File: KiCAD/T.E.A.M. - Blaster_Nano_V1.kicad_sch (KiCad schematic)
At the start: 15 parts, among them J1 USB_C_Receptacle_USB2.0_14P, J2 Conn_01x02, J3 Conn_01x02, J4 Conn_01x02, J5 Conn_01x02, Q1 FS8205A, U1 TP4056-42-ESOP8, U2 DW01A

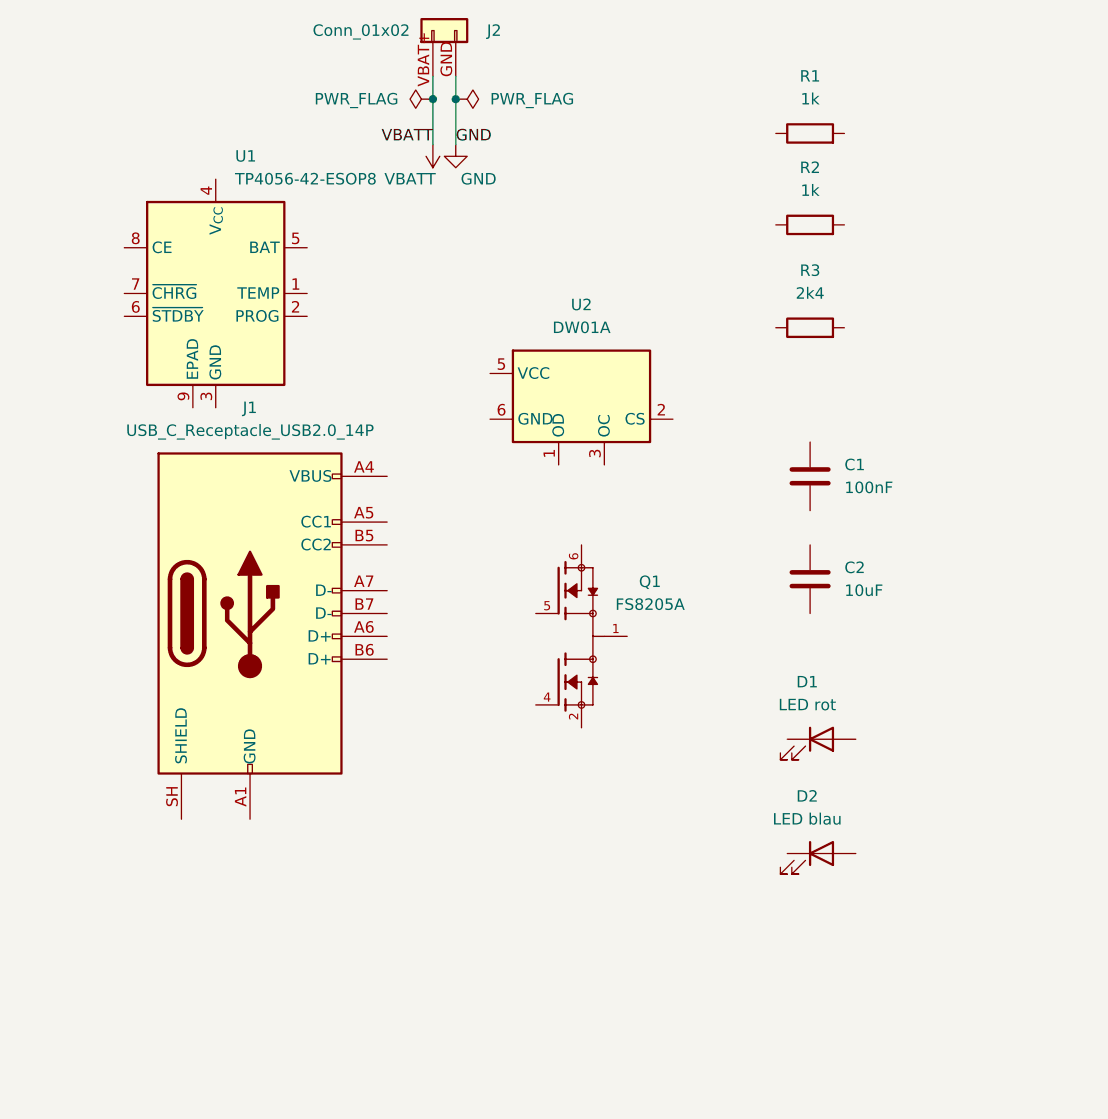
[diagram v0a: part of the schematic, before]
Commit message: Sektor 1 POWER - DW01A verdrahtet.
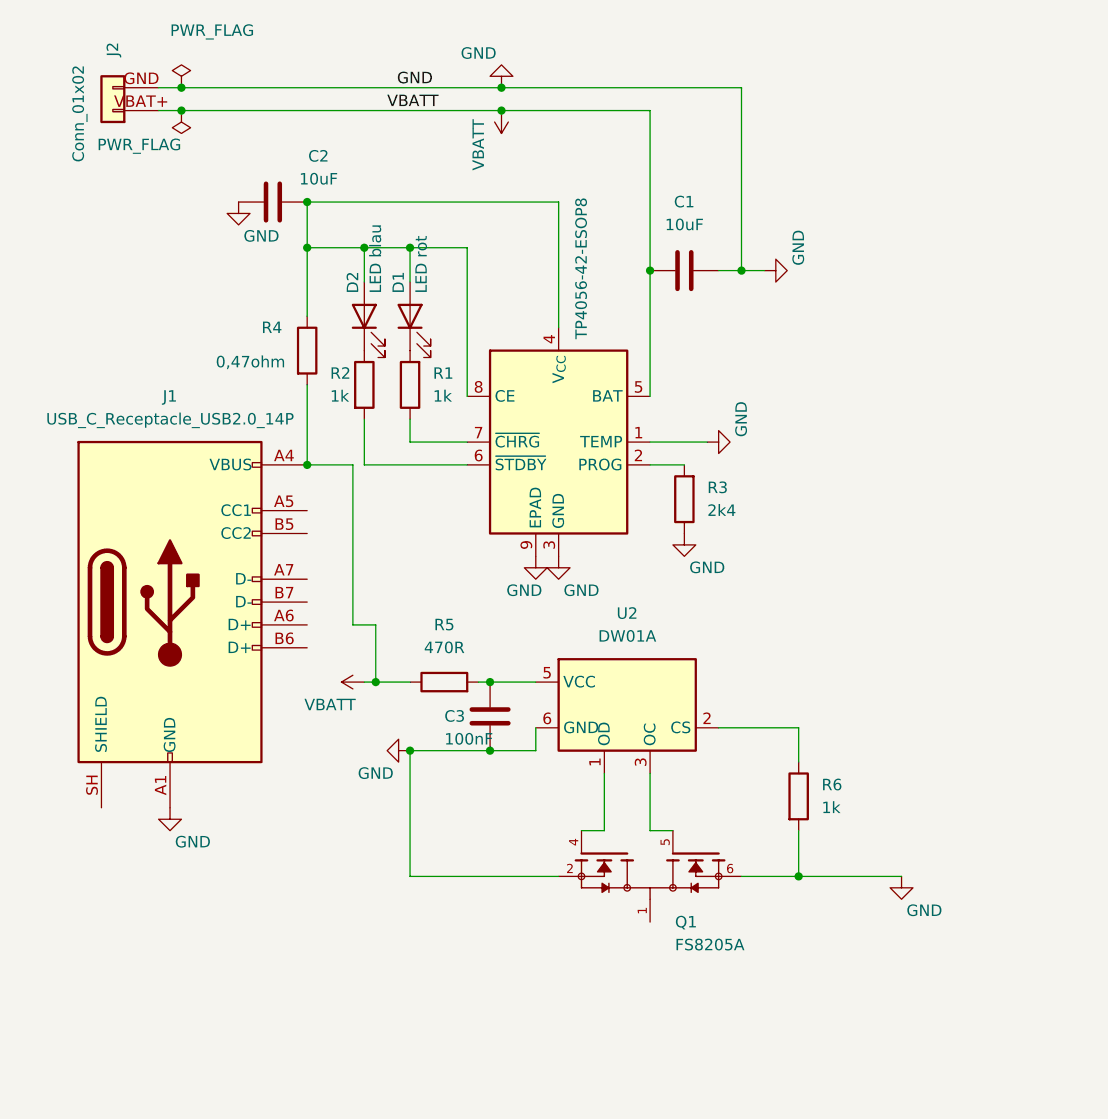
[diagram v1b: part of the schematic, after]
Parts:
- added C3: 100nF, symbol Device:C
- added R4: 0,47ohm, symbol Device:R
- added R5: 470R, symbol Device:R
- added R6: 1k, symbol Device:R
- C1: value 100nF -> 10uF
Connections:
- net GND: now also C1.2, C2.1, J1.A1 (GND), J1.A12 (GND), J1.B1 (GND), J1.B12 (GND), Q1.2, Q1.3, Q1.6, Q1.7, R3.1, U1.1 (TEMP), U1.3 (GND), U1.9 (EPAD), U2.6 (GND), C3.2, R6.2
- net VBATT: now also C1.1, J1.A4 (VBUS), J1.A9 (VBUS), J1.B4 (VBUS), J1.B9 (VBUS), U1.5 (BAT), R4.2, R5.1
- net at R2.1: now also D2.1 (K)
- net at R2.2: now also U1.6 (~{STDBY})
- net at D2.2 (A): now also C2.2, D1.2 (A), U1.4 (V_{CC}), U1.8 (CE), R4.1
- net at R1.1: now also U1.7 (~{CHRG})
- net at R1.2: now also D1.1 (K)
- net at Q1.4: now also U2.1 (OD)
- net at Q1.5: now also U2.3 (OC)
- net at U2.2 (CS): now also R6.1
- net at U2.5 (VCC): now also C3.1, R5.2
- net at R3.2: now also U1.2 (PROG)
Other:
- moved on the sheet: C1, C2, D1, D2, J1, J2, Q1, R1, R2, R3, U2

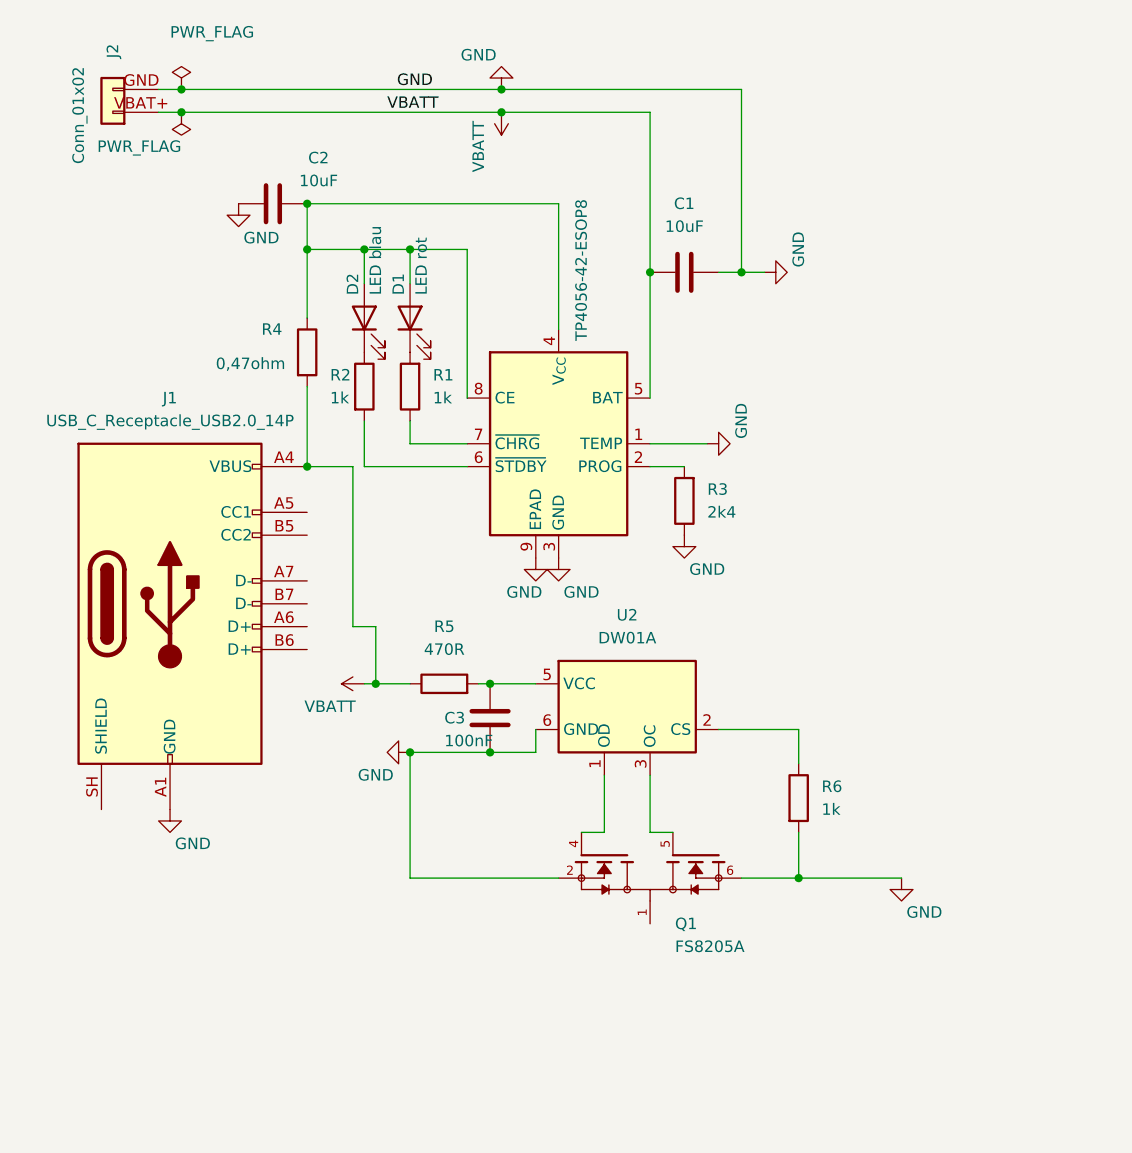
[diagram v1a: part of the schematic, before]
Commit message: Sektor 1 POWER -vollständig verdrahtet und eingerahmt.
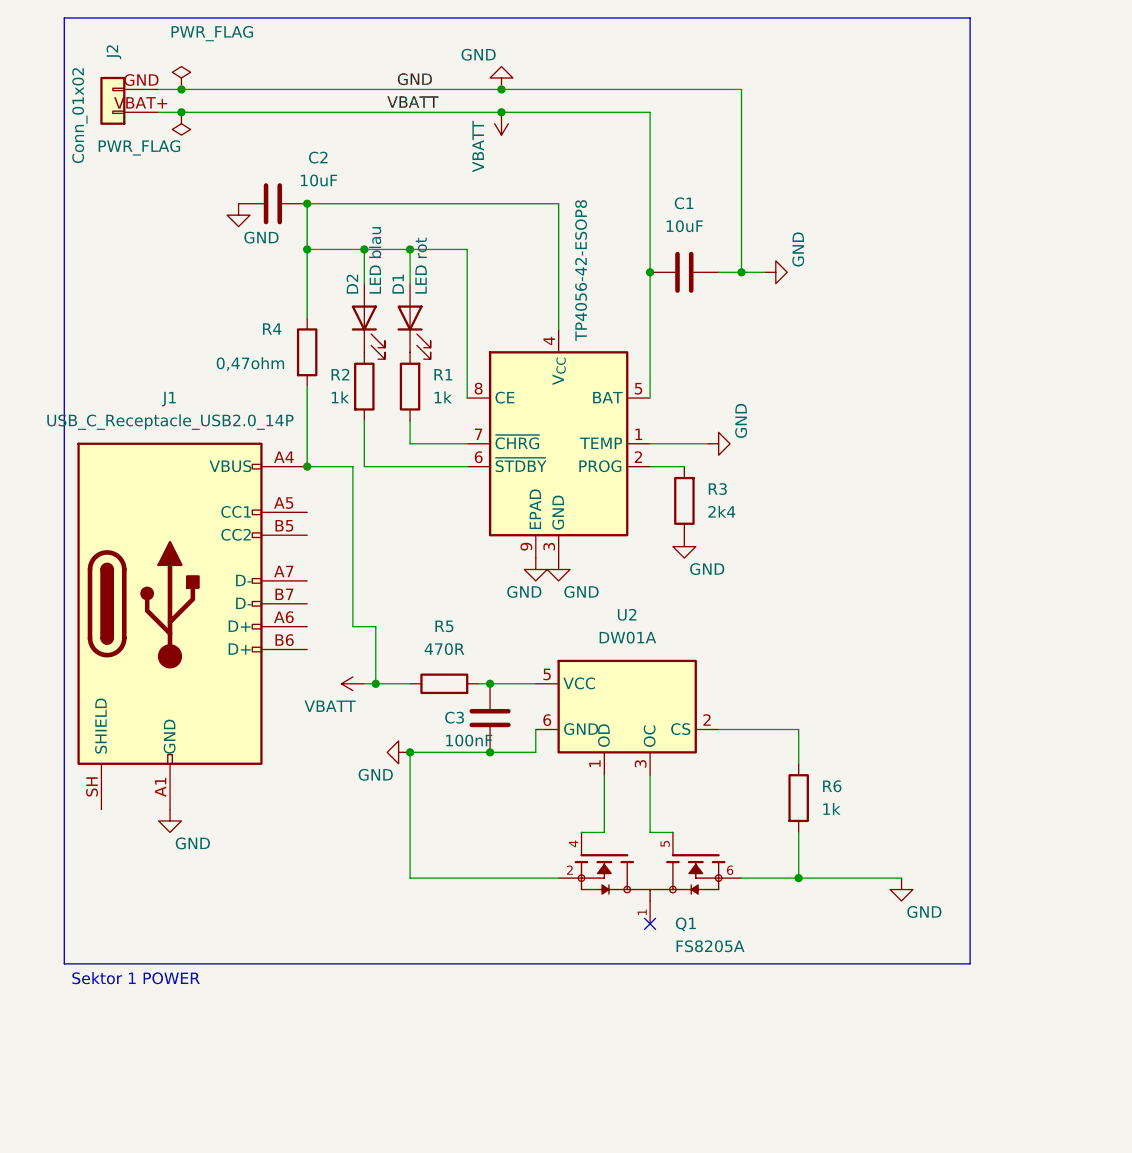
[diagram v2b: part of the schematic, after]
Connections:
- no-connect marks 0 -> 1
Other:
- note added: "Sektor 1 POWER"
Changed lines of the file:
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@@
 		(comment 1 "Thorsten Papendorff")
+	)
+	(rectangle
+		(start 12.3825 12.3825)
+		(end 113.03 117.475)
+		(stroke
+			(width 0)
+			(type default)
+		)
+		(fill
+			(type none)
+		)
+	)
+	(text "Sektor 1 POWER\n"
+		(exclude_from_sim no)
+		(at 20.32 119.38 0)
+		(effects
+			(font
+				(size 1.27 1.27)
+			)
+		)
 	)
 	(junction
@@
 		(color 0 0 0 0)
 	)
+	(no_connect
+		(at 77.47 113.03)
+	)
 	(wire

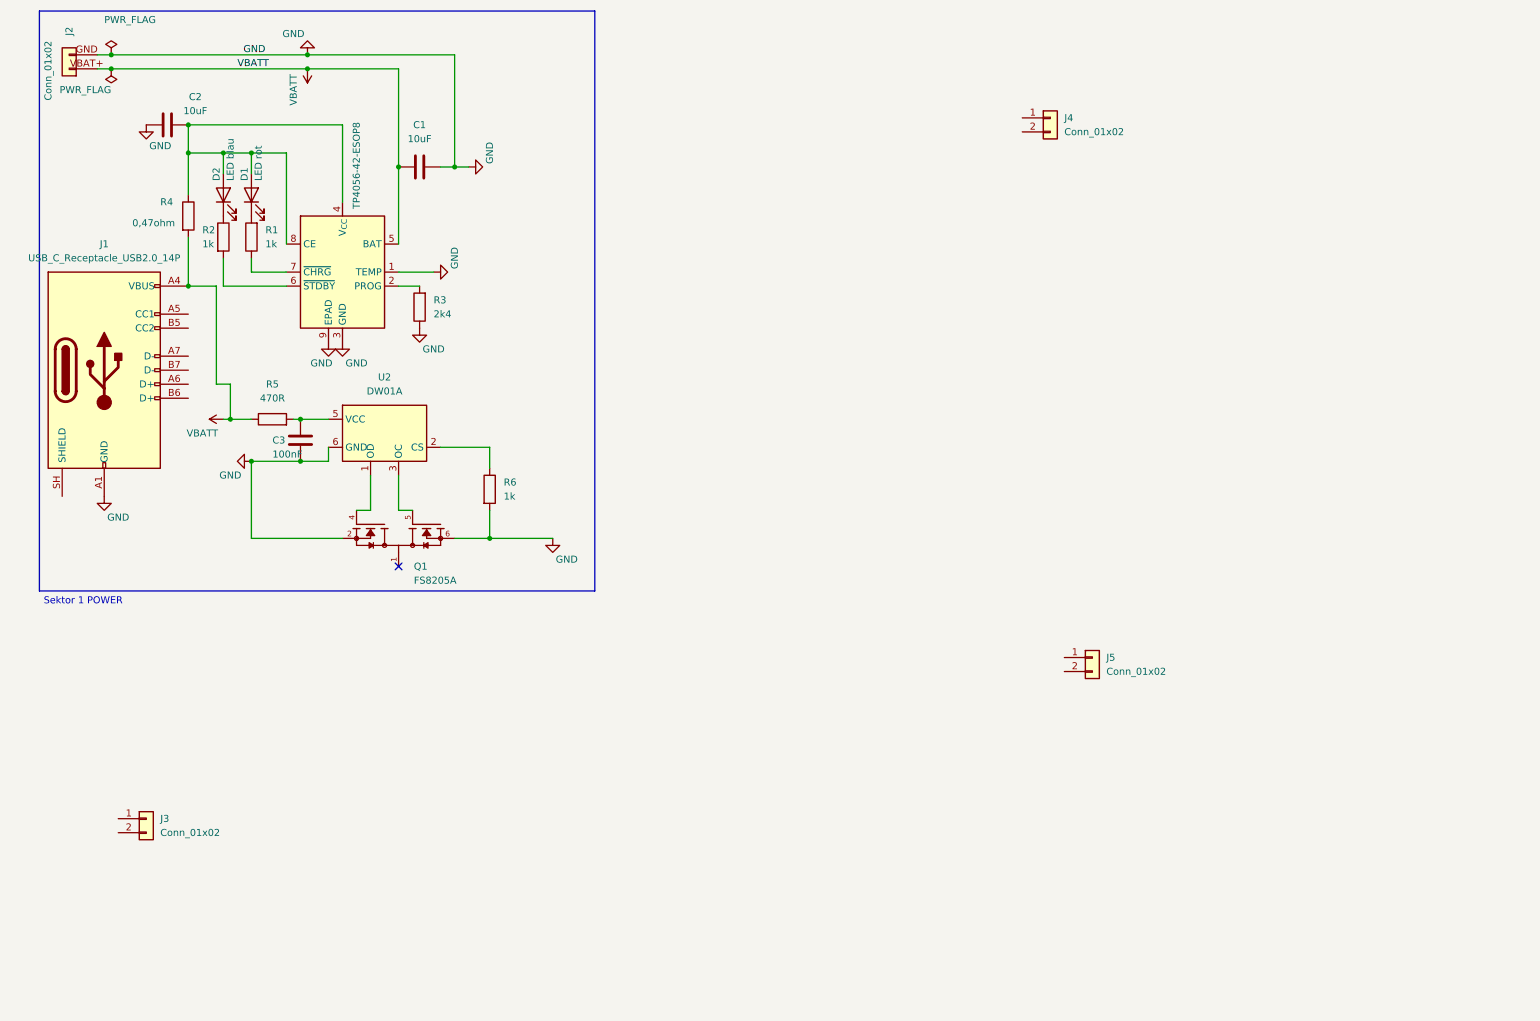
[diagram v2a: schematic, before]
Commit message: Sektor 2 SPANNUNG - MT3608 fertig verdrahtet.
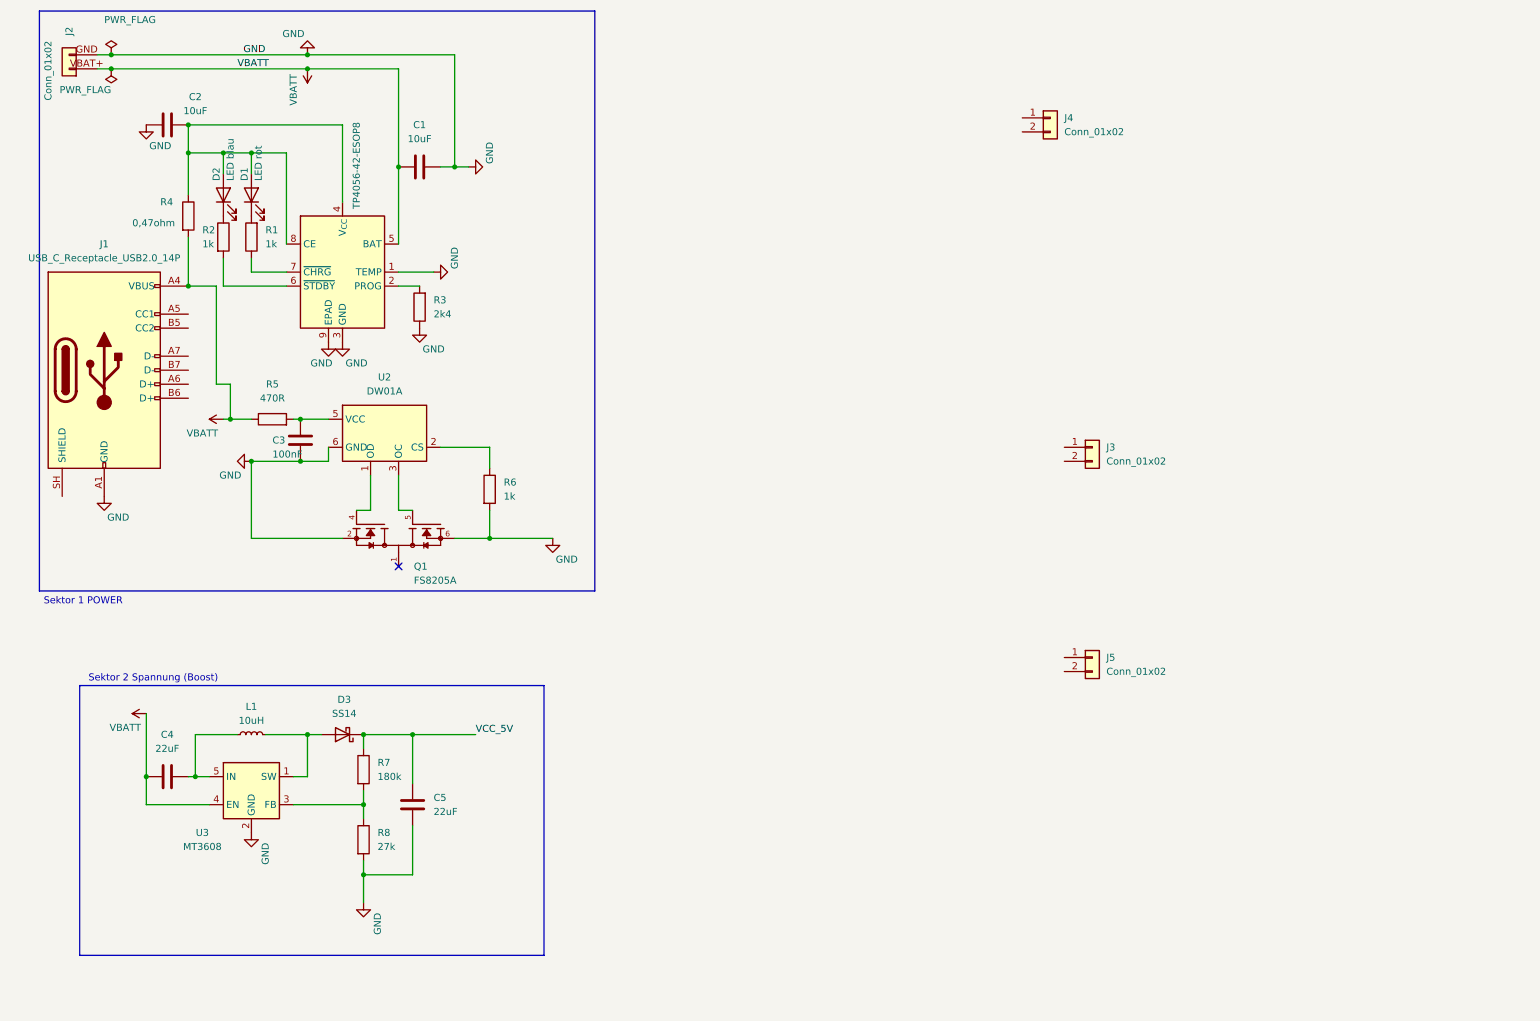
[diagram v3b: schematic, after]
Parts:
- added C4, C5: 22uF, symbol Device:C
- added D3: SS14, Diode_SMD:D_SMA, symbol Diode:SS14
- added L1: 10uH, symbol Device:L_Small
- added R7: 180k, symbol Device:R
- added R8: 27k, symbol Device:R
- added U3: MT3608, Package_TO_SOT_SMD:SOT-23-6, symbol Regulator_Switching:MT3608
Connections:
- net GND: now also C5.2, R8.2, U3.2 (GND)
- net VBATT: now also C4.1, U3.4 (EN)
- new net: C4.2, L1.1, U3.5 (IN)
- new net: D3.2 (A), L1.2, U3.1 (SW)
- new net: R7.2, R8.1, U3.3 (FB)
- new net VCC_5V: C5.1, D3.1 (K), R7.1
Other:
- note added: "Sektor 2 Spannung (Boost)"
- moved on the sheet: J3
